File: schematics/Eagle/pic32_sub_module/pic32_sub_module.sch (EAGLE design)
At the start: 2 parts, among them U1 PIC32MZ2048EFG144-I/PH

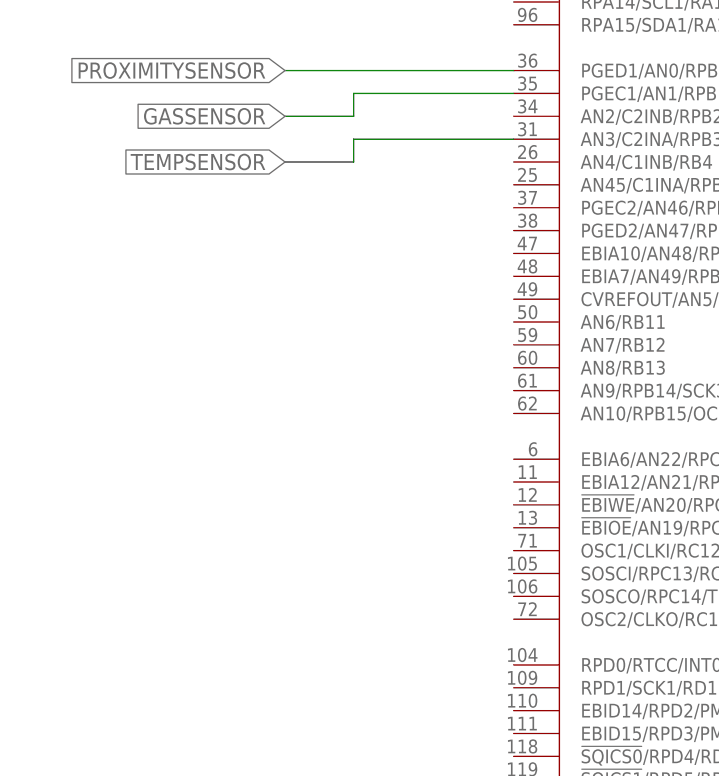
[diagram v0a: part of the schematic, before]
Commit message: updated schematics with pinouts
Added pintout information for motors.
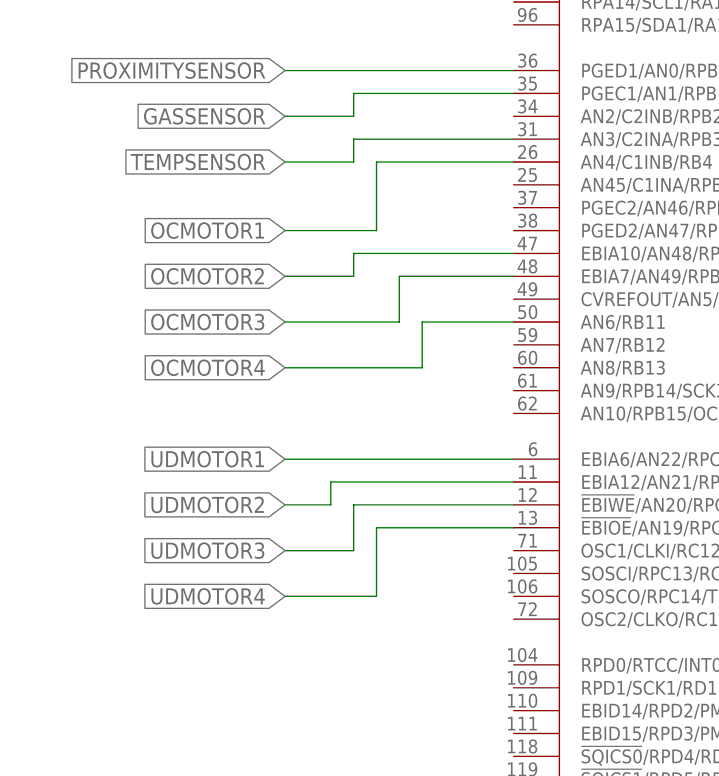
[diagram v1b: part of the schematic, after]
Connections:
- new net OCMOTOR1: U1.AN4/C1INB/RB4
- new net OCMOTOR2: U1.EBIA10/AN48/RPB8/PMA10/RB8
- new net OCMOTOR3: U1.EBIA7/AN49/RPB9/PMA7/RB9
- new net OCMOTOR4: U1.AN6/RB11
- new net UDMOTOR1: U1.EBIA6/AN22/RPC1/PMA6/RC1
- new net UDMOTOR2: U1.EBIA12/AN21/RPC2/PMA12/RC2
- new net UDMOTOR3: U1.!EBIWE!/AN20/RPC3/PMWR/RC3
- new net UDMOTOR4: U1.!EBIOE!/AN19/RPC4/PMRD/RC4
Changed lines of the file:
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@@
 <setting verticaltext="up"/>
 </settings>
-<grid distance="0.1" unitdist="inch" unit="inch" style="lines" multiple="1" display="yes" altdistance="0.01" altunitdist="inch" altunit="inch"/>
+<grid distance="0.1" unitdist="inch" unit="inch" style="lines" multiple="1" display="no" altdistance="0.01" altunitdist="inch" altunit="inch"/>
 <layers>
 <layer number="1" name="Top" color="4" fill="1" visible="no" active="no"/>
@@
 </segment>
 </net>
+<net name="OCMOTOR1" class="0">
+<segment>
+<pinref part="U1" gate="G$1" pin="AN4/C1INB/RB4"/>
+<wire x1="-48.26" y1="60.96" x2="-63.5" y2="60.96" width="0.1524" layer="91"/>
+<wire x1="-63.5" y1="60.96" x2="-63.5" y2="53.34" width="0.1524" layer="91"/>
+<wire x1="-63.5" y1="53.34" x2="-73.66" y2="53.34" width="0.1524" layer="91"/>
+<label x="-73.66" y="53.34" size="1.778" layer="95" rot="R180" xref="yes"/>
+</segment>
+</net>
+<net name="OCMOTOR2" class="0">
+<segment>
+<pinref part="U1" gate="G$1" pin="EBIA10/AN48/RPB8/PMA10/RB8"/>
+<wire x1="-48.26" y1="50.8" x2="-66.04" y2="50.8" width="0.1524" layer="91"/>
+<wire x1="-66.04" y1="50.8" x2="-66.04" y2="48.26" width="0.1524" layer="91"/>
+<wire x1="-66.04" y1="48.26" x2="-73.66" y2="48.26" width="0.1524" layer="91"/>
+<label x="-73.66" y="48.26" size="1.778" layer="95" rot="R180" xref="yes"/>
+</segment>
+</net>
+<net name="OCMOTOR3" class="0">
+<segment>
+<pinref part="U1" gate="G$1" pin="EBIA7/AN49/RPB9/PMA7/RB9"/>
+<wire x1="-48.26" y1="48.26" x2="-60.96" y2="48.26" width="0.1524" layer="91"/>
+<wire x1="-60.96" y1="48.26" x2="-60.96" y2="43.18" width="0.1524" layer="91"/>
+<wire x1="-60.96" y1="43.18" x2="-73.66" y2="43.18" width="0.1524" layer="91"/>
+<label x="-73.66" y="43.18" size="1.778" layer="95" rot="R180" xref="yes"/>
+</segment>
+</net>
+<net name="OCMOTOR4" class="0">
+<segment>
+<wire x1="-58.42" y1="38.1" x2="-73.66" y2="38.1" width="0.1524" layer="91"/>
+<label x="-73.66" y="38.1" size="1.778" layer="95" rot="R180" xref="yes"/>
+<wire x1="-58.42" y1="38.1" x2="-58.42" y2="43.18" width="0.1524" layer="91"/>
+<pinref part="U1" gate="G$1" pin="AN6/RB11"/>
+<wire x1="-58.42" y1="43.18" x2="-48.26" y2="43.18" width="0.1524" layer="91"/>
+</segment>
+</net>
+<net name="UDMOTOR1" class="0">
+<segment>
+<pinref part="U1" gate="G$1" pin="EBIA6/AN22/RPC1/PMA6/RC1"/>
+<wire x1="-48.26" y1="27.94" x2="-73.66" y2="27.94" width="0.1524" layer="91"/>
+<label x="-73.66" y="27.94" size="1.778" layer="95" rot="R180" xref="yes"/>
+</segment>
+</net>
+<net name="UDMOTOR2" class="0">
+<segment>
+<pinref part="U1" gate="G$1" pin="EBIA12/AN21/RPC2/PMA12/RC2"/>
+<wire x1="-48.26" y1="25.4" x2="-68.58" y2="25.4" width="0.1524" layer="91"/>
+<wire x1="-68.58" y1="25.4" x2="-68.58" y2="22.86" width="0.1524" layer="91"/>
+<wire x1="-68.58" y1="22.86" x2="-73.66" y2="22.86" width="0.1524" layer="91"/>
+<label x="-73.66" y="22.86" size="1.778" layer="95" rot="R180" xref="yes"/>
+</segment>
+</net>
+<net name="UDMOTOR3" class="0">
+<segment>
+<pinref part="U1" gate="G$1" pin="!EBIWE!/AN20/RPC3/PMWR/RC3"/>
+<wire x1="-48.26" y1="22.86" x2="-66.04" y2="22.86" width="0.1524" layer="91"/>
+<wire x1="-66.04" y1="22.86" x2="-66.04" y2="17.78" width="0.1524" layer="91"/>
+<wire x1="-66.04" y1="17.78" x2="-73.66" y2="17.78" width="0.1524" layer="91"/>
+<label x="-73.66" y="17.78" size="1.778" layer="95" rot="R180" xref="yes"/>
+</segment>
+</net>
+<net name="UDMOTOR4" class="0">
+<segment>
+<pinref part="U1" gate="G$1" pin="!EBIOE!/AN19/RPC4/PMRD/RC4"/>
+<wire x1="-48.26" y1="20.32" x2="-63.5" y2="20.32" width="0.1524" layer="91"/>
+<wire x1="-63.5" y1="20.32" x2="-63.5" y2="12.7" width="0.1524" layer="91"/>
+<wire x1="-63.5" y1="12.7" x2="-73.66" y2="12.7" width="0.1524" layer="91"/>
+<label x="-73.66" y="12.7" size="1.778" layer="95" rot="R180" xref="yes"/>
+</segment>
+</net>
